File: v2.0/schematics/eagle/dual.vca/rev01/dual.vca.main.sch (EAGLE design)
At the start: 36 parts, among them IC1 TL084P, IC2 TL082P, Q1 2N3417, Q2 2N3417, Q3 2N3417

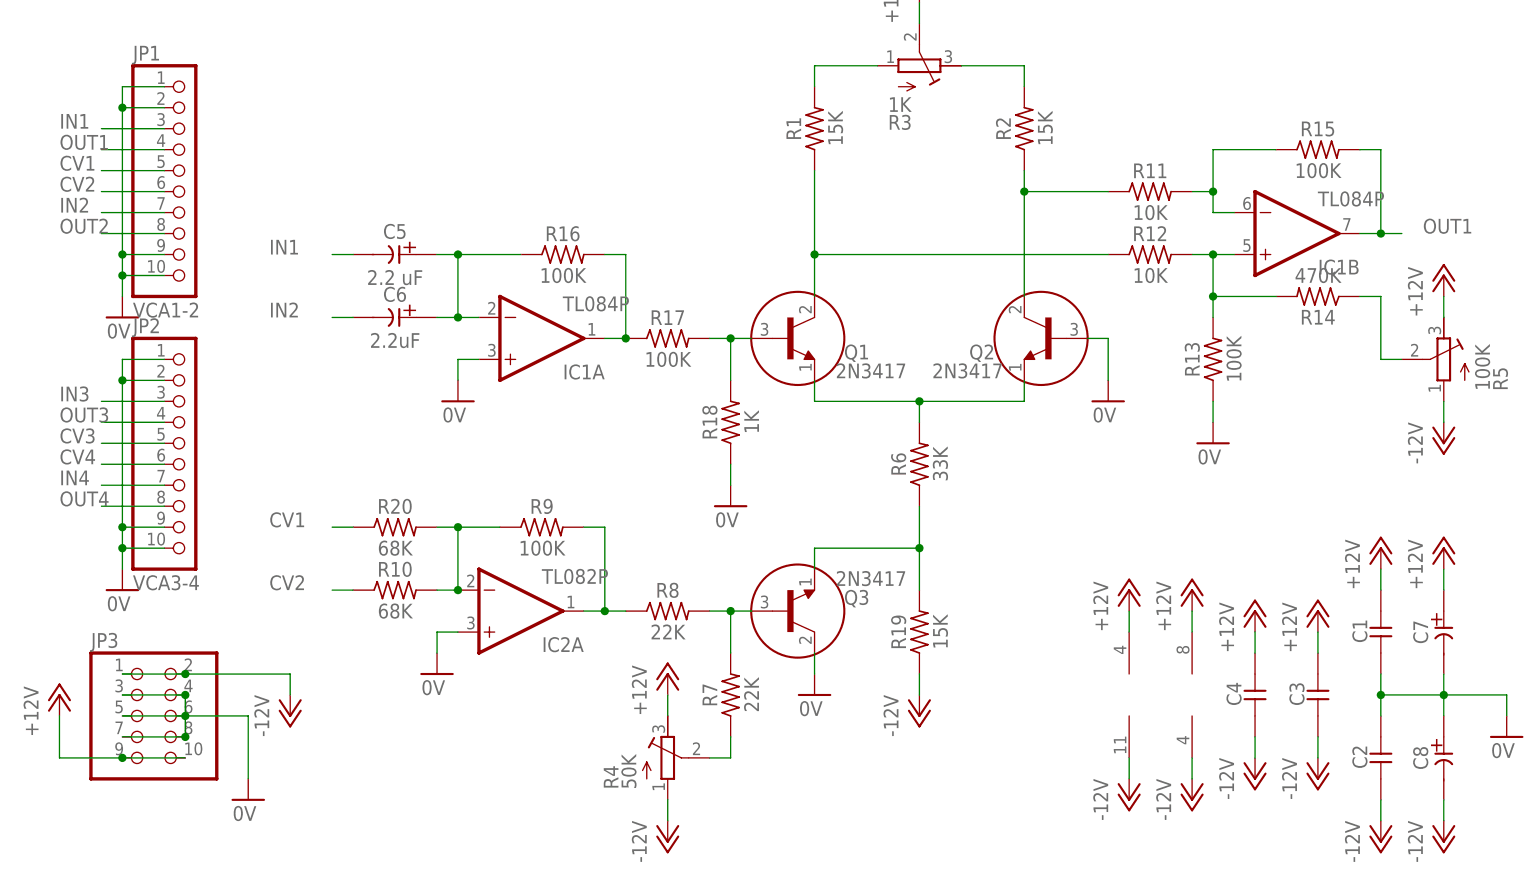
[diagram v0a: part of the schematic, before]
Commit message: Updated dual.vca values
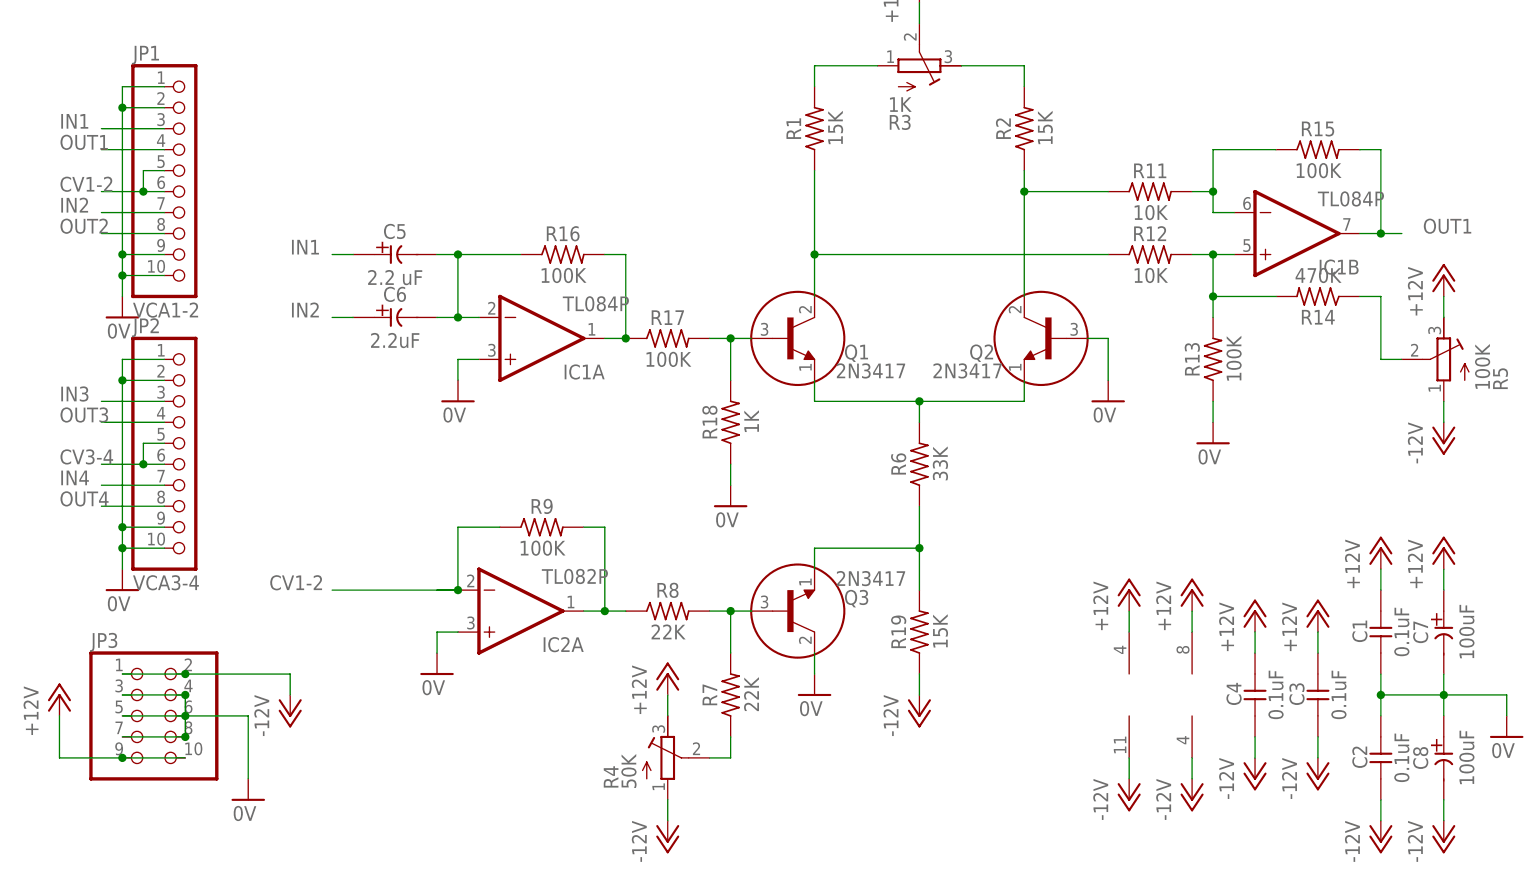
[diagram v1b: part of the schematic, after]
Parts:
- removed R10, R20: 68K, _common:R
- C1, C2, C3, C4: value (none) -> 0.1uF
- C7, C8: value (none) -> 100uF
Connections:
- removed net CV1: JP1.5, R20.1
- removed net CV2: JP1.6, R10.1
- removed net CV3: JP2.5
- removed net CV4: JP2.6
- removed net N$18: IC2A.-IN, R10.2, R20.2, R9.1
- new net CV1-2: IC2A.-IN, JP1.5, JP1.6, R9.1
- new net CV3-4: JP2.5, JP2.6
- net IN1: now also C5.+; no longer C5.-
- net IN2: now also C6.+; no longer C6.-
- net N$1: now also C5.-, C6.-; no longer C5.+, C6.+
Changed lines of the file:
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@@
 <?xml version="1.0" encoding="utf-8"?>
 <!DOCTYPE eagle SYSTEM "eagle.dtd">
-<eagle version="9.5.1">
+<eagle version="9.6.2">
 <drawing>
 <settings>
@@
 <part name="GND1" library="supply1" library_urn="urn:adsk.eagle:library:371" deviceset="0V" device=""/>
 <part name="JP3" library="pinhead" library_urn="urn:adsk.eagle:library:325" deviceset="PINHD-2X5" device="" package3d_urn="urn:adsk.eagle:package:22470/2"/>
-<part name="C1" library="_common" deviceset="CC-US" device="025-024X044"/>
-<part name="C2" library="_common" deviceset="CC-US" device="025-024X044"/>
-<part name="C3" library="_common" deviceset="CC-US" device="025-024X044"/>
-<part name="C4" library="_common" deviceset="CC-US" device="025-024X044"/>
+<part name="C1" library="_common" deviceset="CC-US" device="025-024X044" value="0.1uF"/>
+<part name="C2" library="_common" deviceset="CC-US" device="025-024X044" value="0.1uF"/>
+<part name="C3" library="_common" deviceset="CC-US" device="025-024X044" value="0.1uF"/>
+<part name="C4" library="_common" deviceset="CC-US" device="025-024X044" value="0.1uF"/>
 <part name="C5" library="_common" deviceset="CE-US" device="E2-5" value="2.2 uF"/>
 <part name="C6" library="_common" deviceset="CE-US" device="E2-5" value="2.2uF"/>
-<part name="C7" library="_common" deviceset="CE-US" device="E2-5"/>
-<part name="C8" library="_common" deviceset="CE-US" device="E2-5"/>
+<part name="C7" library="_common" deviceset="CE-US" device="E2-5" value="100uF"/>
+<part name="C8" library="_common" deviceset="CE-US" device="E2-5" value="100uF"/>
 <part name="R6" library="_common" deviceset="R" device="" value="33K"/>
 <part name="GND2" library="supply1" library_urn="urn:adsk.eagle:library:371" deviceset="0V" device=""/>
@@
 <part name="R8" library="_common" deviceset="R" device="" value="22K"/>
 <part name="R9" library="_common" deviceset="R" device="" value="100K"/>
-<part name="R10" library="_common" deviceset="R" device="" value="68K"/>
 <part name="GND5" library="supply1" library_urn="urn:adsk.eagle:library:371" deviceset="0V" device=""/>
 <part name="R11" library="_common" deviceset="R" device="" value="10K"/>
@@
 <part name="P-10" library="supply1" library_urn="urn:adsk.eagle:library:371" deviceset="-12V" device=""/>
 <part name="GND8" library="supply1" library_urn="urn:adsk.eagle:library:371" deviceset="0V" device=""/>
-<part name="R20" library="_common" deviceset="R" device="" value="68K"/>
 </parts>
 <sheets>
@@
 <attribute name="VALUE" x="142.24" y="15.24" size="1.778" layer="96" rot="R90" align="center"/>
 </instance>
-<instance part="C5" gate="G$1" x="35.56" y="68.58" smashed="yes" rot="R270">
-<attribute name="NAME" x="35.56" y="71.374" size="1.778" layer="95" align="center"/>
-<attribute name="VALUE" x="35.56" y="65.786" size="1.778" layer="96" align="center"/>
-</instance>
-<instance part="C6" gate="G$1" x="35.56" y="60.96" smashed="yes" rot="R270">
-<attribute name="NAME" x="35.56" y="63.754" size="1.778" layer="95" align="center"/>
-<attribute name="VALUE" x="35.56" y="58.166" size="1.778" layer="96" align="center"/>
+<instance part="C5" gate="G$1" x="35.56" y="68.58" smashed="yes" rot="MR270">
+<attribute name="NAME" x="35.56" y="71.374" size="1.778" layer="95" rot="MR0" align="center"/>
+<attribute name="VALUE" x="35.56" y="65.786" size="1.778" layer="96" rot="MR0" align="center"/>
+</instance>
+<instance part="C6" gate="G$1" x="35.56" y="60.96" smashed="yes" rot="MR270">
+<attribute name="NAME" x="35.56" y="63.754" size="1.778" layer="95" rot="MR0" align="center"/>
+<attribute name="VALUE" x="35.56" y="58.166" size="1.778" layer="96" rot="MR0" align="center"/>
 </instance>
 <instance part="C7" gate="G$1" x="162.56" y="22.86" smashed="yes">
@@
 <attribute name="NAME" x="53.34" y="38.0746" size="1.778" layer="95" align="center"/>
 <attribute name="VALUE" x="53.34" y="33.02" size="1.778" layer="96" align="center"/>
-</instance>
-<instance part="R10" gate="G$1" x="35.56" y="27.94" smashed="yes">
-<attribute name="NAME" x="35.56" y="30.4546" size="1.778" layer="95" align="center"/>
-<attribute name="VALUE" x="35.56" y="25.4" size="1.778" layer="96" align="center"/>
 </instance>
 <instance part="GND5" gate="1" x="40.64" y="17.78" smashed="yes">
@@
 <instance part="GND8" gate="1" x="134.62" y="45.72" smashed="yes">
 <attribute name="VALUE" x="132.715" y="43.18" size="1.778" layer="96"/>
-</instance>
-<instance part="R20" gate="G$1" x="35.56" y="35.56" smashed="yes">
-<attribute name="NAME" x="35.56" y="38.0746" size="1.778" layer="95" align="center"/>
-<attribute name="VALUE" x="35.56" y="33.02" size="1.778" layer="96" align="center"/>
 </instance>
 </instances>
@@
 </segment>
 <segment>
-<pinref part="C5" gate="G$1" pin="-"/>
+<pinref part="C5" gate="G$1" pin="+"/>
 <wire x1="30.48" y1="68.58" x2="27.94" y2="68.58" width="0.1524" layer="91"/>
-<label x="20.32" y="68.58" size="1.778" layer="95"/>
+<label x="22.86" y="68.58" size="1.778" layer="95"/>
 </segment>
 </net>
@@
 </segment>
 </net>
-<net name="CV1" class="0">
+<net name="CV1-2" class="0">
+<segment>
+<label x="20.32" y="27.94" size="1.778" layer="95"/>
+<pinref part="R9" gate="G$1" pin="1"/>
+<wire x1="48.26" y1="35.56" x2="43.18" y2="35.56" width="0.1524" layer="91"/>
+<pinref part="IC2" gate="A" pin="-IN"/>
+<wire x1="43.18" y1="35.56" x2="43.18" y2="27.94" width="0.1524" layer="91"/>
+<wire x1="40.64" y1="27.94" x2="43.18" y2="27.94" width="0.1524" layer="91"/>
+<junction x="43.18" y="27.94"/>
+<wire x1="27.94" y1="27.94" x2="43.18" y2="27.94" width="0.1524" layer="91"/>
+</segment>
 <segment>
 <pinref part="JP1" gate="A" pin="5"/>
-<wire x1="7.62" y1="78.74" x2="0" y2="78.74" width="0.1524" layer="91"/>
-<label x="-5.08" y="78.74" size="1.778" layer="95"/>
-</segment>
-<segment>
-<pinref part="R20" gate="G$1" pin="1"/>
-<wire x1="30.48" y1="35.56" x2="27.94" y2="35.56" width="0.1524" layer="91"/>
-<label x="20.32" y="35.56" size="1.778" layer="95"/>
-</segment>
-</net>
-<net name="CV2" class="0">
-<segment>
+<wire x1="7.62" y1="78.74" x2="5.08" y2="78.74" width="0.1524" layer="91"/>
 <pinref part="JP1" gate="A" pin="6"/>
-<wire x1="7.62" y1="76.2" x2="0" y2="76.2" width="0.1524" layer="91"/>
+<wire x1="7.62" y1="76.2" x2="5.08" y2="76.2" width="0.1524" layer="91"/>
 <label x="-5.08" y="76.2" size="1.778" layer="95"/>
-</segment>
-<segment>
-<pinref part="R10" gate="G$1" pin="1"/>
-<wire x1="30.48" y1="27.94" x2="27.94" y2="27.94" width="0.1524" layer="91"/>
-<label x="20.32" y="27.94" size="1.778" layer="95"/>
+<wire x1="5.08" y1="76.2" x2="0" y2="76.2" width="0.1524" layer="91"/>
+<wire x1="5.08" y1="78.74" x2="5.08" y2="76.2" width="0.1524" layer="91"/>
+<junction x="5.08" y="76.2"/>
 </segment>
 </net>
@@
 </segment>
 <segment>
-<pinref part="C6" gate="G$1" pin="-"/>
+<pinref part="C6" gate="G$1" pin="+"/>
 <wire x1="30.48" y1="60.96" x2="27.94" y2="60.96" width="0.1524" layer="91"/>
-<label x="20.32" y="60.96" size="1.778" layer="95"/>
+<label x="22.86" y="60.96" size="1.778" layer="95"/>
 </segment>
 </net>
@@
 <wire x1="7.62" y1="48.26" x2="0" y2="48.26" width="0.1524" layer="91"/>
 <label x="-5.08" y="48.26" size="1.778" layer="95"/>
-</segment>
-</net>
-<net name="CV3" class="0">
-<segment>
-<pinref part="JP2" gate="A" pin="5"/>
-<wire x1="7.62" y1="45.72" x2="0" y2="45.72" width="0.1524" layer="91"/>
-<label x="-5.08" y="45.72" size="1.778" layer="95"/>
-</segment>
-</net>
-<net name="CV4" class="0">
-<segment>
-<pinref part="JP2" gate="A" pin="6"/>
-<wire x1="7.62" y1="43.18" x2="0" y2="43.18" width="0.1524" layer="91"/>
-<label x="-5.08" y="43.18" size="1.778" layer="95"/>
 </segment>
 </net>
@@
 <net name="N$1" class="0">
 <segment>
-<pinref part="C5" gate="G$1" pin="+"/>
 <pinref part="R16" gate="G$1" pin="1"/>
-<wire x1="40.64" y1="68.58" x2="43.18" y2="68.58" width="0.1524" layer="91"/>
 <wire x1="43.18" y1="68.58" x2="50.8" y2="68.58" width="0.1524" layer="91"/>
 <wire x1="43.18" y1="68.58" x2="43.18" y2="60.96" width="0.1524" layer="91"/>
-<junction x="43.18" y="68.58"/>
 <pinref part="IC1" gate="A" pin="-IN"/>
 <wire x1="45.72" y1="60.96" x2="43.18" y2="60.96" width="0.1524" layer="91"/>
-<pinref part="C6" gate="G$1" pin="+"/>
+<pinref part="C5" gate="G$1" pin="-"/>
+<wire x1="40.64" y1="68.58" x2="43.18" y2="68.58" width="0.1524" layer="91"/>
+<junction x="43.18" y="68.58"/>
+<pinref part="C6" gate="G$1" pin="-"/>
 <wire x1="40.64" y1="60.96" x2="43.18" y2="60.96" width="0.1524" layer="91"/>
 <junction x="43.18" y="60.96"/>
@@
 </segment>
 </net>
-<net name="N$18" class="0">
-<segment>
-<pinref part="R9" gate="G$1" pin="1"/>
-<wire x1="48.26" y1="35.56" x2="43.18" y2="35.56" width="0.1524" layer="91"/>
-<pinref part="IC2" gate="A" pin="-IN"/>
-<wire x1="43.18" y1="35.56" x2="43.18" y2="27.94" width="0.1524" layer="91"/>
-<pinref part="R10" gate="G$1" pin="2"/>
-<wire x1="40.64" y1="27.94" x2="43.18" y2="27.94" width="0.1524" layer="91"/>
-<junction x="43.18" y="27.94"/>
-<pinref part="R20" gate="G$1" pin="2"/>
-<wire x1="40.64" y1="35.56" x2="43.18" y2="35.56" width="0.1524" layer="91"/>
-<junction x="43.18" y="35.56"/>
-</segment>
-</net>
+<net name="CV3-4" class="0">
+<segment>
+<pinref part="JP2" gate="A" pin="5"/>
+<wire x1="7.62" y1="45.72" x2="5.08" y2="45.72" width="0.1524" layer="91"/>
+<pinref part="JP2" gate="A" pin="6"/>
+<wire x1="7.62" y1="43.18" x2="5.08" y2="43.18" width="0.1524" layer="91"/>
+<label x="-5.08" y="43.18" size="1.778" layer="95"/>
+<wire x1="5.08" y1="43.18" x2="0" y2="43.18" width="0.1524" layer="91"/>
+<wire x1="5.08" y1="45.72" x2="5.08" y2="43.18" width="0.1524" layer="91"/>
+<junction x="5.08" y="43.18"/>
+</segment>
+</net>
